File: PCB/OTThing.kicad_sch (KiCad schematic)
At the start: 52 parts, among them IC2 TPS61041, J3 USB_C_Receptacle_USB2.0, SW1 RST/CONFIG, SW2 BOOT, U1 ESP32-C3-WROOM-02, U2 AMS1117-3.3, U5 USBLC6-2SC6

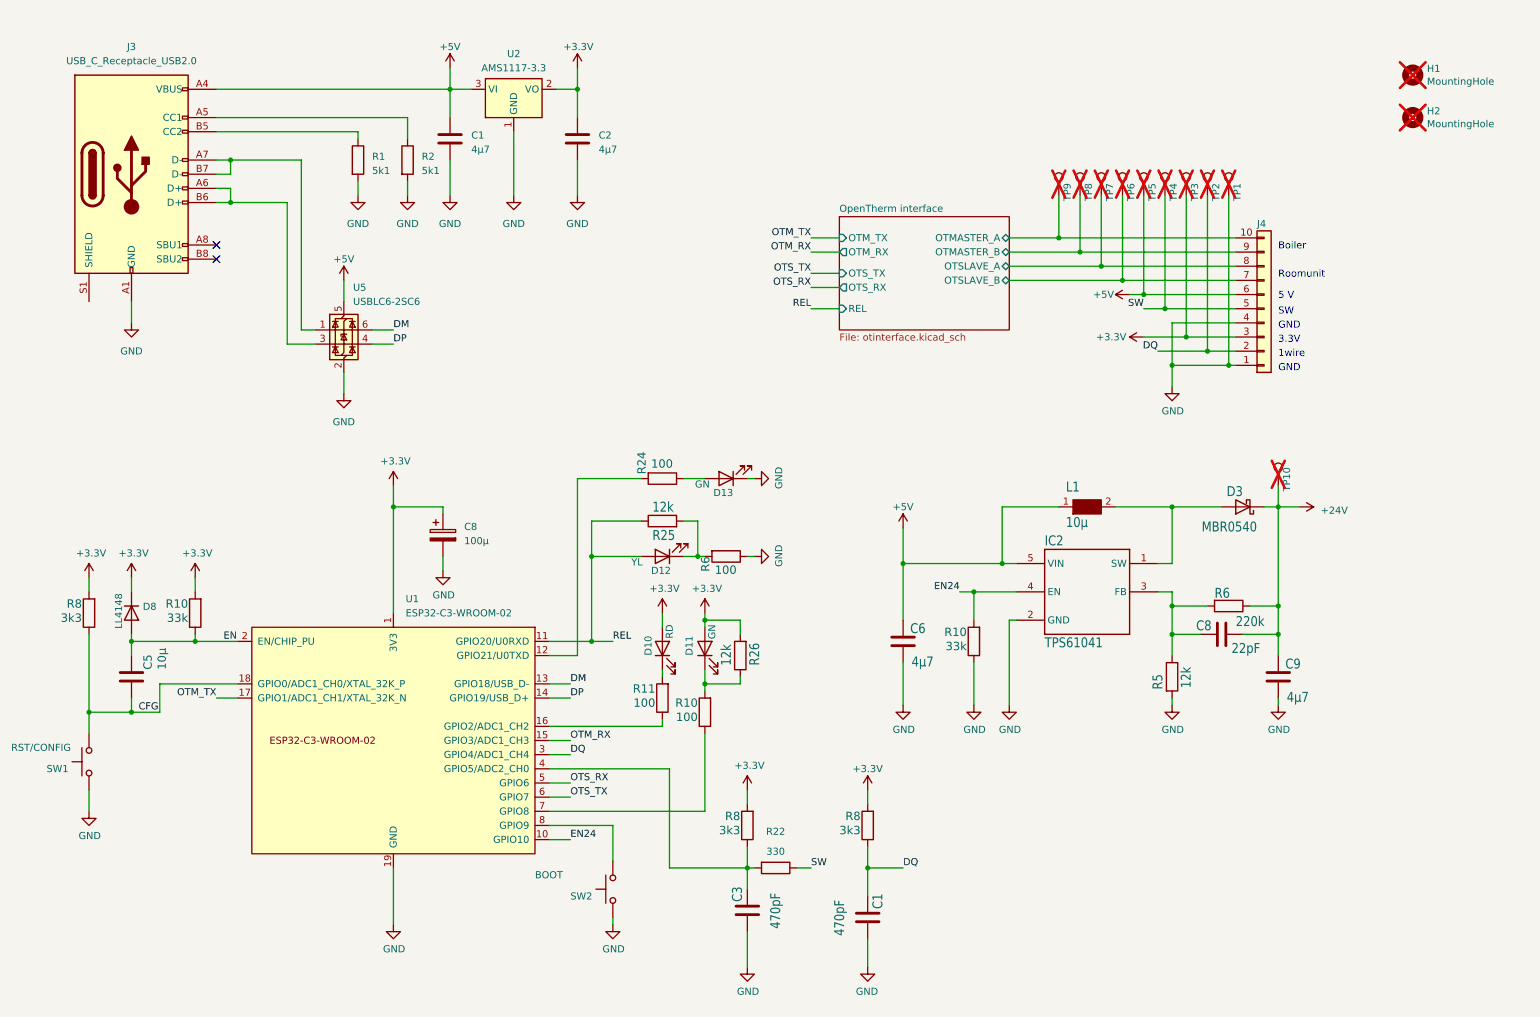
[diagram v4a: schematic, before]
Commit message: add LED for +24V enable
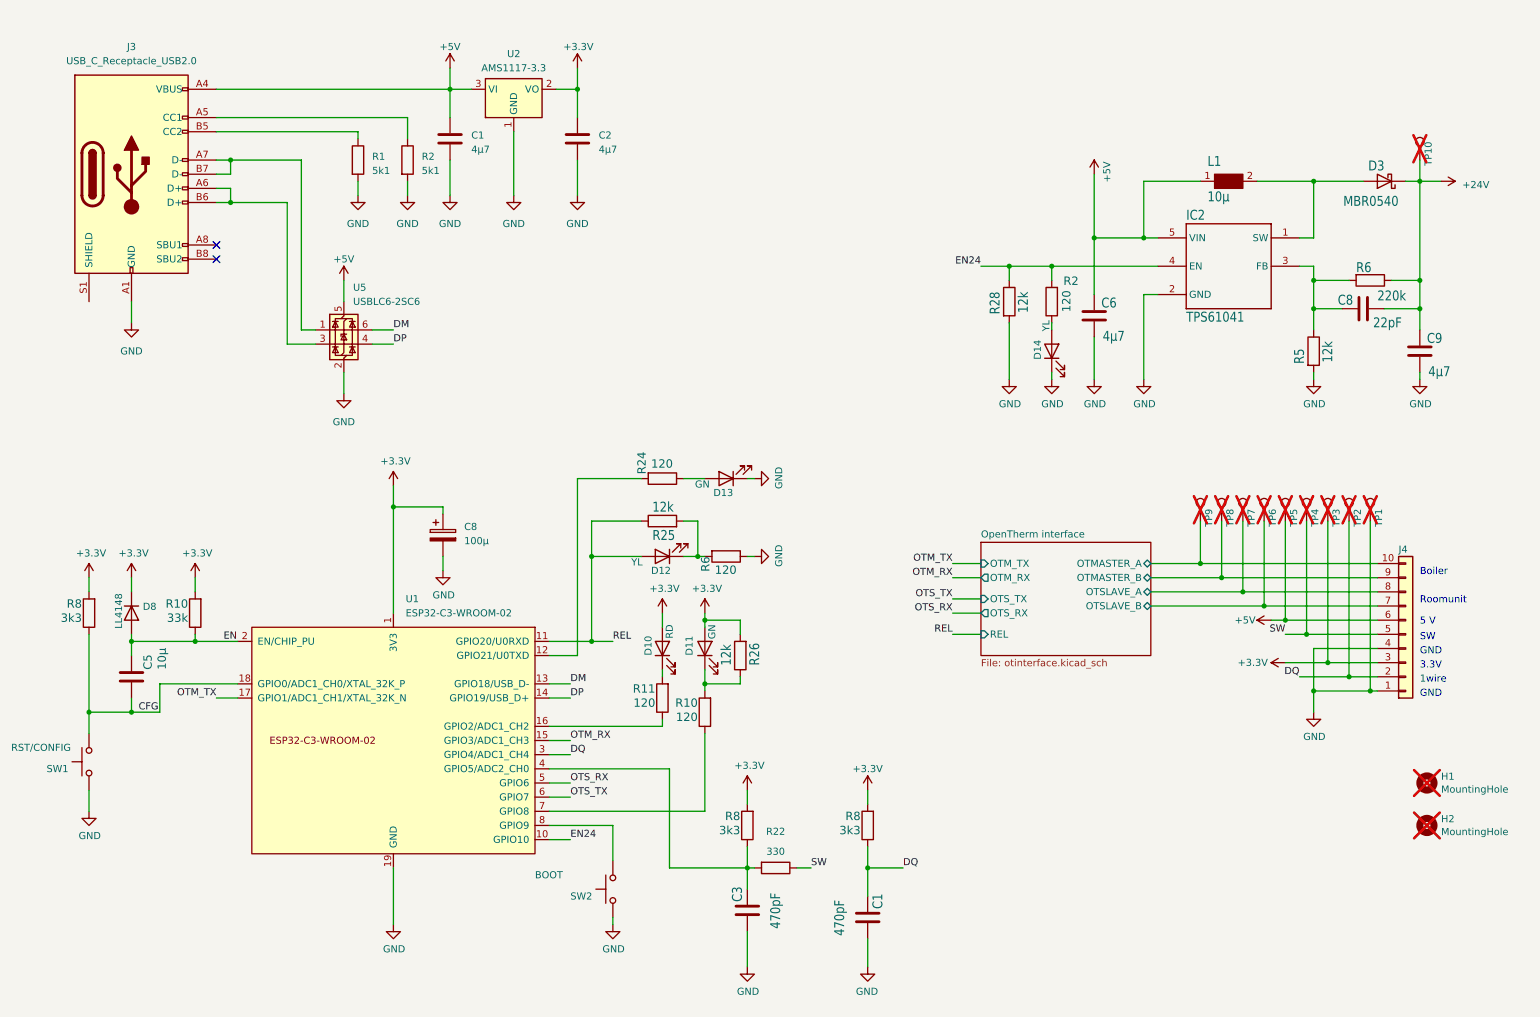
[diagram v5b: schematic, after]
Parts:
- removed R10: 33k, Resistor_SMD:R_0805_2012Metric, symbol Device:R
- added D14: YL, LED_SMD:LED_0805_2012Metric, symbol Device:LED
- added R2: 120, Resistor_SMD:R_0805_2012Metric, symbol Device:R
- added R28: 12k, Resistor_SMD:R_0805_2012Metric, symbol Device:R
- R10, R11, R24, R6: value 100 -> 120; LCSC C17408 -> C17437
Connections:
- net EN24: now also R2.2, R28.1
- net GND: now also D14.1 (K), R28.2
- new net: D14.2 (A), R2.1
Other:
- moved on the sheet: C6, C8, C9, D3, H1, H2, IC2, J4, L1, R5, R6, TP1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

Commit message: migrate to pioarduino smart power add more OT values new partitiontable
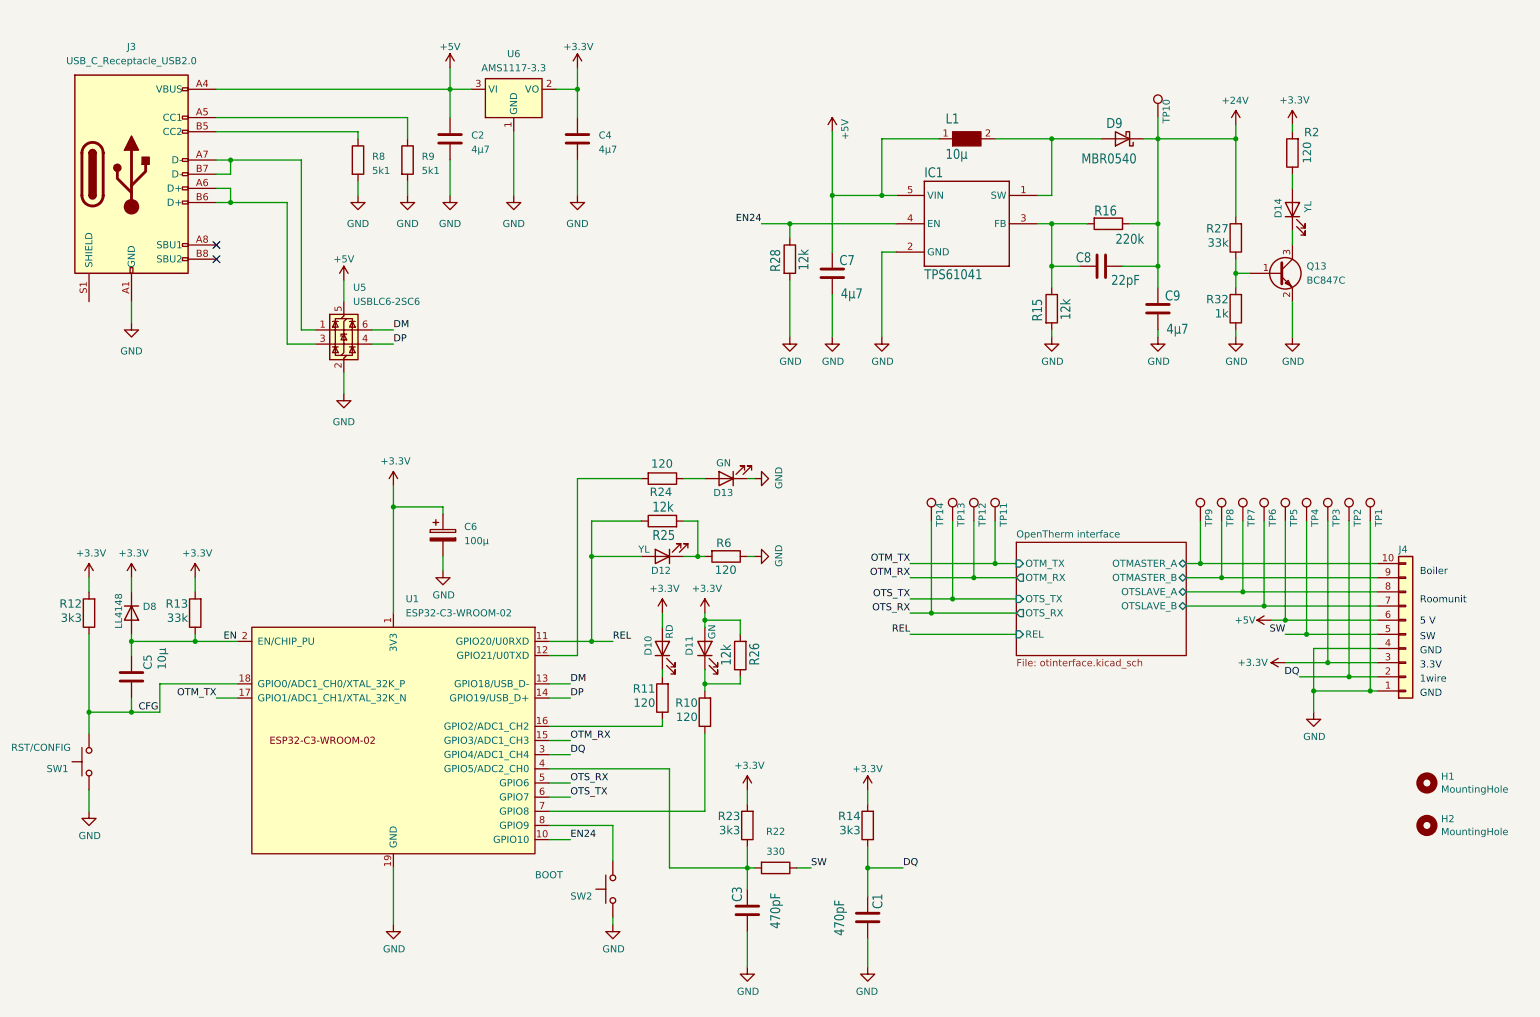
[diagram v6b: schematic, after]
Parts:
- added Q13: BC847C, Package_TO_SOT_SMD:SOT-23, symbol Transistor_BJT:BC847
- added R27: 33k, Resistor_SMD:R_0805_2012Metric, symbol Device:R
- added R32: 1k, Resistor_SMD:R_0805_2012Metric, symbol Device:R
- added TP11, TP12, TP13, TP14: ~, TestPoint:TestPoint_THTPad_D1.5mm_Drill0.7mm, symbol Connector:TestPoint
- H1, H2, TP1, TP10, TP2, TP3, TP4, TP5, TP6, TP7, TP8, TP9: now fitted; now left out of the parts list
- renumbered C1 to C2, C2 to C4, C8 to C6, C6 to C7, D3 to D9, IC2 to IC1, R8 to R12, R10 to R13, R8 to R14, R5 to R15, R6 to R16, R8 to R23, R1 to R8, R2 to R9, U2 to U6
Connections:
- net +24V: now also R27.2
- net +3.3V: now also R2.2
- net EN24: no longer R2.2
- net GND: now also Q13.2 (E), R32.1; no longer D14.1 (K)
- net OTM_RX: now also TP12.1
- net OTM_TX: now also TP11.1
- net OTS_RX: now also TP14.1
- net OTS_TX: now also TP13.1
- new net: Q13.1 (B), R27.1, R32.2
- new net: D14.1 (K), Q13.3 (C)
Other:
- moved on the sheet: C7, C8, C9, D9, IC1, L1, R15, R16, R28

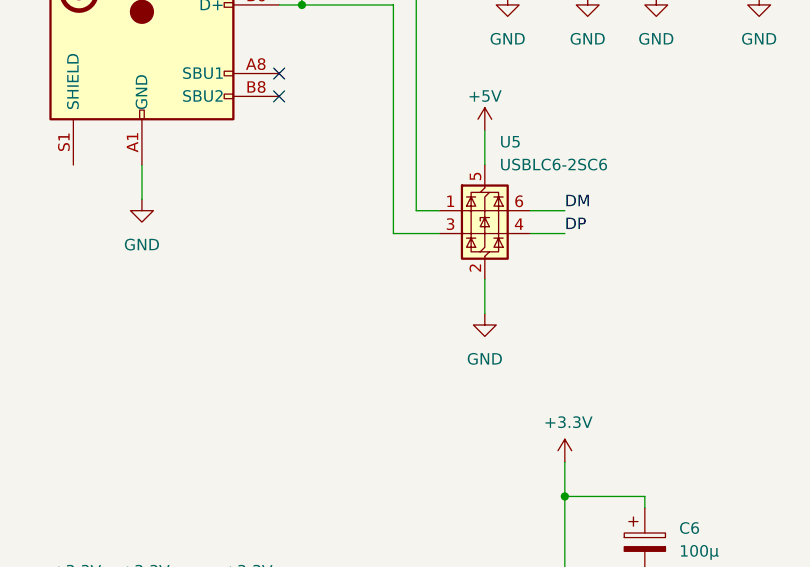
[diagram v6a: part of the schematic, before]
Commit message: add USB test points single board test w/ power supply
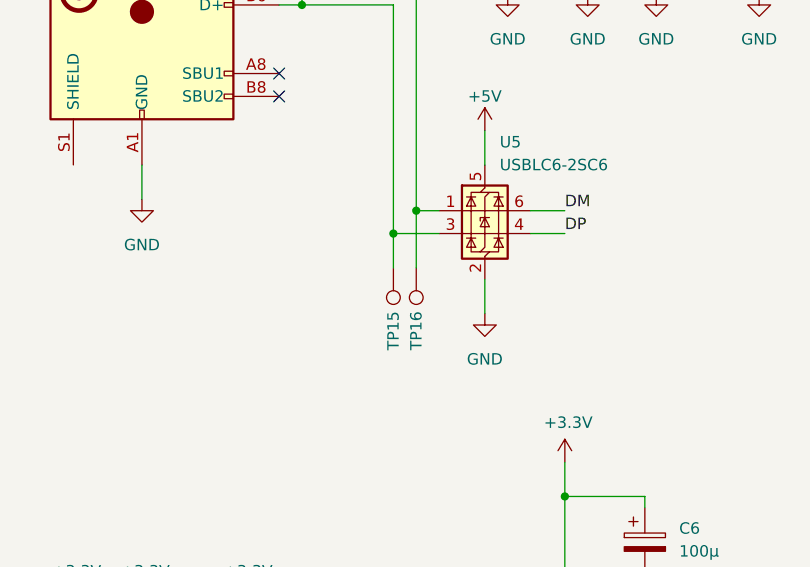
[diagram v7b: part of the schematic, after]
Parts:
- added TP15, TP16: ~, TestPoint:TestPoint_THTPad_D1.5mm_Drill0.7mm, symbol Connector:TestPoint
- D11, D13: LCSC C965847 -> C965815
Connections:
- net at J3.A7 (D-), J3.B7 (D-), U5.1 (I/O1): now also TP16.1
- net at J3.A6 (D+), J3.B6 (D+), U5.3 (I/O2): now also TP15.1
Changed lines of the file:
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@@
 	)
 	(junction
+		(at 64.77 72.39)
+		(diameter 0)
+		(color 0 0 0 0)
+	)
+	(junction
 		(at 181.61 120.65)
 		(diameter 0)
@@
 	)
 	(junction
+		(at 62.23 74.93)
+		(diameter 0)
+		(color 0 0 0 0)
+	)
+	(junction
 		(at 248.92 132.08)
 		(diameter 0)
@@
 	(wire
 		(pts
+			(xy 62.23 74.93) (xy 62.23 78.74)
+		)
+		(stroke
+			(width 0)
+			(type default)
+		)
+	)
+	(wire
+		(pts
 			(xy 74.93 36.83) (xy 74.93 38.1)
 		)
@@
 	(wire
 		(pts
+			(xy 64.77 72.39) (xy 64.77 78.74)
+		)
+		(stroke
+			(width 0)
+			(type default)
+		)
+	)
+	(wire
+		(pts
 			(xy 152.4 53.34) (xy 171.45 53.34)
 		)
@@
 			)
 		)
-		(property "LCSC" "C965847"
+		(property "LCSC" "C965815"
 			(at 137.16 129.54 0)
 			(effects
@@
 	)
 	(symbol
+		(lib_id "Connector:TestPoint")
+		(at 62.23 78.74 180)
+		(unit 1)
+		(exclude_from_sim no)
+		(in_bom no)
+		(on_board yes)
+		(dnp no)
+		(property "Reference" "TP15"
+			(at 62.23 83.566 90)
+			(effects
+				(font
+					(size 1.27 1.27)
+				)
+				(justify left)
+			)
+		)
+		(property "Value" "~"
+			(at 59.69 80.7721 0)
+			(effects
+				(font
+					(size 1.27 1.27)
+				)
+				(justify left)
+			)
+		)
+		(property "Footprint" "TestPoint:TestPoint_THTPad_D1.5mm_Drill0.7mm"
+			(at 57.15 78.74 0)
+			(effects
+				(font
+					(size 1.27 1.27)
+				)
+				(hide yes)
+			)
+		)
+		(property "Datasheet" "~"
+			(at 57.15 78.74 0)
+			(effects
+				(font
+					(size 1.27 1.27)
+				)
+				(hide yes)
+			)
+		)
+		(property "Description" "test point"
+			(at 62.23 78.74 0)
+			(effects
+				(font
+					(size 1.27 1.27)
+				)
+				(hide yes)
+			)
+		)
+		(pin "1"
+		)
+		(instances
+			(project "OTThing"
+				(path "/cb61f12f-ab02-48e5-a06c-10aea7e452c9"
+					(reference "TP15")
+					(unit 1)
+				)
+			)
+		)
+	)
+	(symbol
 		(lib_id "power:GND")
 		(at 83.82 48.26 0)
@@
 	)
 	(symbol
+		(lib_id "Connector:TestPoint")
+		(at 64.77 78.74 180)
+		(unit 1)
+		(exclude_from_sim no)
+		(in_bom no)
+		(on_board yes)
+		(dnp no)
+		(property "Reference" "TP16"
+			(at 64.77 83.566 90)
+			(effects
+				(font
+					(size 1.27 1.27)
+				)
+				(justify left)
+			)
+		)
+		(property "Value" "~"
+			(at 62.23 80.7721 0)
+			(effects
+				(font
+					(size 1.27 1.27)
+				)
+				(justify left)
+			)
+		)
+		(property "Footprint" "TestPoint:TestPoint_THTPad_D1.5mm_Drill0.7mm"
+			(at 59.69 78.74 0)
+			(effects
+				(font
+					(size 1.27 1.27)
+				)
+				(hide yes)
+			)
+		)
+		(property "Datasheet" "~"
+			(at 59.69 78.74 0)
+			(effects
+				(font
+					(size 1.27 1.27)
+				)
+				(hide yes)
+			)
+		)
+		(property "Description" "test point"
+			(at 64.77 78.74 0)
+			(effects
+				(font
+					(size 1.27 1.27)
+				)
+				(hide yes)
+			)
+		)
+		(pin "1"
+		)
+		(instances
+			(project "OTThing"
+				(path "/cb61f12f-ab02-48e5-a06c-10aea7e452c9"
+					(reference "TP16")
+					(unit 1)
+				)
+			)
+		)
+	)
+	(symbol
 		(lib_id "Connector:USB_C_Receptacle_USB2.0")
 		(at 34.29 44.45 0)
@@
 			)
 		)
-		(property "LCSC" "C965847"
+		(property "LCSC" "C965815"
 			(at 140.97 99.06 0)
 			(effects

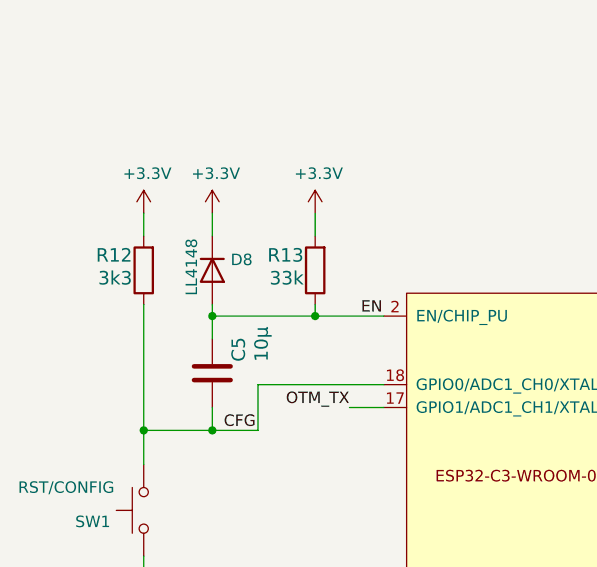
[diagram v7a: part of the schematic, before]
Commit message: change TVS diodes
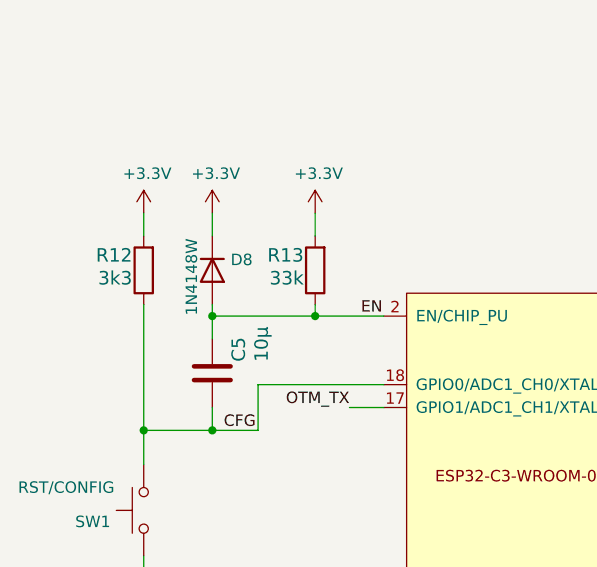
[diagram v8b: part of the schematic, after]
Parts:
- D8: value LL4148 -> 1N4148W; footprint Diode_SMD:D_MiniMELF -> Diode_SMD:D_SOD-123; LCSC C435829 -> (none)
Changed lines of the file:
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@@
 			)
 		)
-		(property "Value" "LL4148"
+		(property "Value" "1N4148W"
 			(at 32.004 119.634 0)
 			(effects
@@
 			)
 		)
-		(property "Footprint" "Diode_SMD:D_MiniMELF"
+		(property "Footprint" "Diode_SMD:D_SOD-123"
 			(at 29.845 123.19 0)
 			(effects
@@
 			)
 		)
-		(property "LCSC" "C435829"
+		(property "LCSC" ""
 			(at 34.29 123.19 0)
 			(effects
